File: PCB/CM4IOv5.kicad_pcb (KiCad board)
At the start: 6 copper layers, 80.9 x 63 mm, 67 parts, among them CN1 DF40C-100DS-0.4V(51), CN2 DF40C-100DS-0.4V(51), J1 Micro_SD_Card_Det, J2 Conn_01x02_Pin, J4 Conn_01x22_Female, J5 Conn_01x22_Female, U1 QG2439S, U2 74LVC1G07SE-7, U3 AP2331SA-7, U4 RT9742GGJ5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

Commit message: Routed EEPROM modules to SDA/SCL and GPIO pins.
These are definitely taking up more space than they need to, but a little extra space will provide easier in-situ changes if rewiring is needed.
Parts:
- removed R7: 523k, Resistor_SMD:R_0603_1608Metric
- removed R8: 84.5, Resistor_SMD:R_0603_1608Metric
- added U6: M24C64-WMN6TP, PARTS:SOIC-8_L5.0-W4.0-P1.27-LS6.0-BL, B.Cu at (429.3, 176.5)
- added U7: M24C64-WMN6TP, PARTS:SOIC-8_L5.0-W4.0-P1.27-LS6.0-BL, B.Cu at (418.8, 176.5)
- added U8: 74LVC1G125GV-TP, PARTS:SOT-23-5_L2.9-W1.6-P0.95-LS2.8-BR, B.Cu at (418.6, 172.0)
- added U9: 74LVC1G125GV-TP, PARTS:SOT-23-5_L2.9-W1.6-P0.95-LS2.8-BR, B.Cu at (429.5, 172.0)
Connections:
- RJ2 pad 5: /CM4_GPIO ( Ethernet, GPIO, SDCARD)/BI_DB- -> /CM4_GPIO ( Ethernet, GPIO, SDCARD)/BI_DC-
- RJ2 pad 6: Net-(RJ2-Pad6) -> /CM4_GPIO ( Ethernet, GPIO, SDCARD)/BI_DB-
- U1 pad 17: Net-(RJ2-Pad6) -> /CM4_GPIO ( Ethernet, GPIO, SDCARD)/BI_DB-
- U1 pad 20: /CM4_GPIO ( Ethernet, GPIO, SDCARD)/BI_DB- -> /CM4_GPIO ( Ethernet, GPIO, SDCARD)/BI_DC-
- U5 pad : (no net) -> GND
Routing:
- net /CM4_GPIO ( Ethernet, GPIO, SDCARD)/GPIO21: track 0.00 -> 47.6 mm, vias 0 -> 3
- net /CM4_HighSpeed/SDA0: track 60.5 -> 103.1 mm, vias 4 -> 9
- net /CM4_HighSpeed/SCL0: track 61.2 -> 101.8 mm, vias 4 -> 7
- net /CM4_GPIO ( Ethernet, GPIO, SDCARD)/GPIO25: track 0.00 -> 40.2 mm, vias 0 -> 3
- net /+3.3v: track 38.8 -> 70.6 mm, vias 10 -> 21
- net Net-(RJ2-Pad6): track 30.2 -> 0.00 mm, vias 1 -> 0
- net /CM4_GPIO ( Ethernet, GPIO, SDCARD)/BI_DC-: track 0.00 -> 23.8 mm
- net /CM4_GPIO ( Ethernet, GPIO, SDCARD)/ID_SC: track 89.8 -> 103.7 mm, vias 6 -> 9
- net /CM4_GPIO ( Ethernet, GPIO, SDCARD)/ID_SD: track 81.7 -> 93.5 mm, vias 3 -> 6
- net GND: track 172.6 -> 182.5 mm, vias 182 -> 169
- net Net-(U5-EN): track 7.31 -> 0.00 mm
- net /CM4_GPIO ( Ethernet, GPIO, SDCARD)/nPWR_LED: track 56.8 -> 63.9 mm
- net /CM4_GPIO ( Ethernet, GPIO, SDCARD)/BI_DB-: track 23.8 -> 30.2 mm, vias 0 -> 1
- net /CM4_GPIO ( Ethernet, GPIO, SDCARD)/PROM1_WC: track 0.00 -> 5.34 mm
- net /CM4_GPIO ( Ethernet, GPIO, SDCARD)/PROM0_WC: track 0.00 -> 5.13 mm
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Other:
- board text added: "PROM0"
- board text added: "PROM1"

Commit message: Updated fonts for export.
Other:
- board text added: "PROM_1"
- board text added: "PROM_Zero"
- board text removed: "PROM0"
- board text removed: "PROM1"

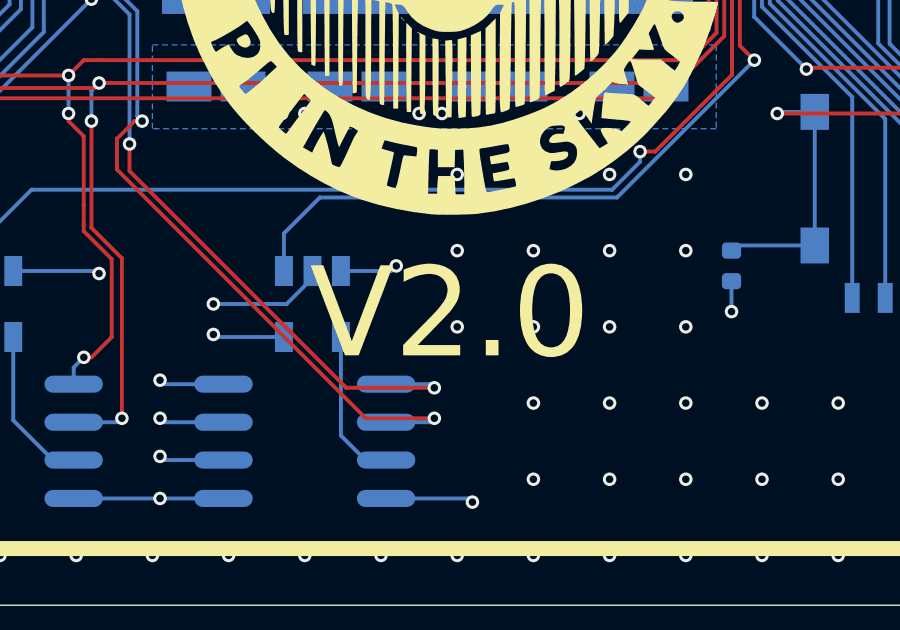
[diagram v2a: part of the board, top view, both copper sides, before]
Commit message: Updated silkscreen for release.
Exported STEP/JLC Production Files.
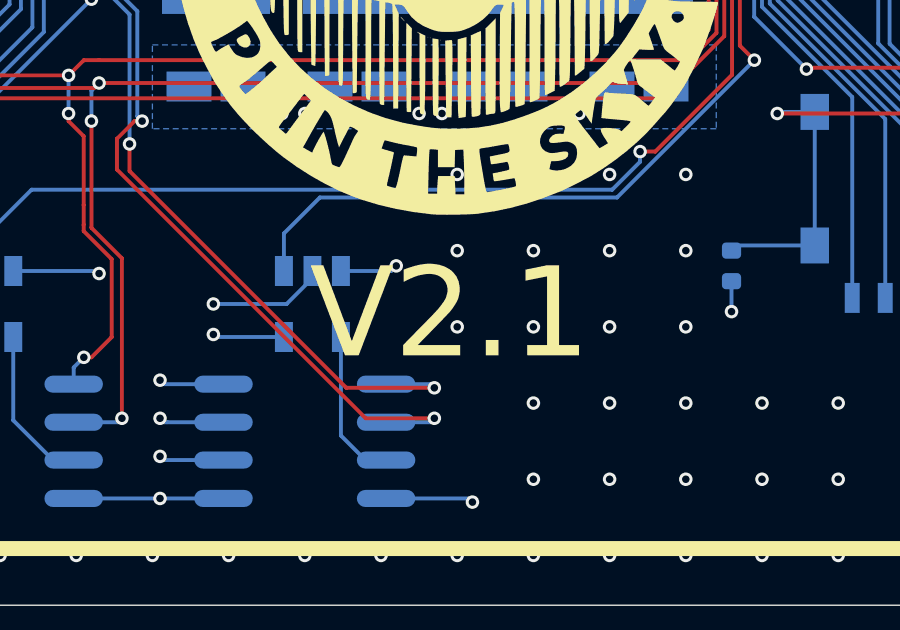
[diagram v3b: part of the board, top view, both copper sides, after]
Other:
- board text added: "V2.1"
- board text removed: "V2.0"
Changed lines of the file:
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@@
 			(pintype "unspecified")
 		)
-		(model "/PARTS.3dshapes/SOIC-8_L4.9-W3.9-H1.7-LS6.0-P1.27.wrl"
+		(model "${PARTS_3D_FILES}/SOIC-8_L4.9-W3.9-H1.7-LS6.0-P1.27.step"
 			(offset
 				(xyz 0 0 -0)
@@
 			(pintype "unspecified")
 		)
-		(model "/PARTS.3dshapes/SOIC-8_L4.9-W3.9-H1.7-LS6.0-P1.27.wrl"
+		(model "${PARTS_3D_FILES}/SOIC-8_L4.9-W3.9-H1.7-LS6.0-P1.27.step"
 			(offset
 				(xyz 0 0 -0)
@@
 		)
 	)
-	(gr_text "V2.0"
-		(at 407.065222 169.82 -0)
+	(gr_text "V2.1"
+		(at 407.065222 169.82 0)
 		(layer "B.SilkS" knockout)
 		(effects
@@
 			(justify mirror)
 		)
-		(render_cache "V2.0" -0
+		(render_cache "V2.1" 0
 			(polygon
 				(pts
@@
 			(polygon
 				(pts
-					(xy 403.960467 167.834354) (xy 404.113928 167.861041) (xy 404.263267 167.910603) (xy 404.358201 167.955574)
-					(xy 404.489783 168.039174) (xy 404.608382 168.142145) (xy 404.679823 168.221051) (xy 404.770498 168.349542)
-					(xy 404.84139 168.490191) (xy 404.876652 168.588881) (xy 404.910656 168.741552) (xy 404.92199 168.899787)
-					(xy 404.92199 170.041378) (xy 404.916952 170.147532) (xy 404.890505 170.302298) (xy 404.84139 170.451706)
-					(xy 404.796327 170.546502) (xy 404.712246 170.678737) (xy 404.608382 170.799019) (xy 404.530759 170.869819)
-					(xy 404.403504 170.959876) (xy 404.263267 171.030561) (xy 404.164165 171.066144) (xy 404.012078 171.100457)
-					(xy 403.85587 171.111894) (xy 403.751319 171.106811) (xy 403.598098 171.080123) (xy 403.449206 171.030561)
-					(xy 403.353951 170.985453) (xy 403.22206 170.901132) (xy 403.103358 170.796821) (xy 403.031962 170.717961)
-					(xy 402.941528 170.589711) (xy 402.871083 170.449508) (xy 402.8355 170.350635) (xy 402.801187 170.198376)
-					(xy 402.78975 170.041378) (xy 402.78975 168.924699) (xy 403.209603 168.924699) (xy 403.209603 170.022327)
-					(xy 403.214344 170.10868) (xy 403.246769 170.256182) (xy 403.309913 170.393482) (xy 403.403776 170.520582)
-					(xy 403.44062 170.559211) (xy 403.558027 170.652302) (xy 403.70058 170.715628) (xy 403.85587 170.736737)
-					(xy 403.903801 170.734837) (xy 404.055384 170.701063) (xy 404.194373 170.625071) (xy 404.308696 170.520582)
-					(xy 404.364424 170.451231) (xy 404.440931 170.318464) (xy 404.486835 170.175496) (xy 404.502136 170.022327)
-					(xy 404.502136 168.924699) (xy 404.497378 168.838486) (xy 404.46483 168.690784) (xy 404.401448 168.552704)
-					(xy 404.307231 168.424246) (xy 404.270145 168.384962) (xy 404.152396 168.290294) (xy 404.010144 168.225894)
-					(xy 403.85587 168.204427) (xy 403.808326 168.206353) (xy 403.657658 168.240585) (xy 403.519012 168.317607)
-					(xy 403.404509 168.423513) (xy 403.348359 168.493323) (xy 403.271273 168.626914) (xy 403.225021 168.770706)
-					(xy 403.209603 168.924699) (xy 402.78975 168.924699) (xy 402.78975 168.899787) (xy 402.794833 168.793678)
-					(xy 402.82152 168.639153) (xy 402.871083 168.490191) (xy 402.915825 168.395074) (xy 402.999596 168.26253)
-					(xy 403.103358 168.142145) (xy 403.181027 168.071345) (xy 403.308522 167.981289) (xy 403.449206 167.910603)
-					(xy 403.547986 167.87502) (xy 403.699764 167.840708) (xy 403.85587 167.82927)
+					(xy 403.974572 168.315069) (xy 404.025863 168.251322) (xy 404.458905 168.251322) (xy 404.36072 167.876165)
+					(xy 403.924014 167.876165) (xy 403.778845 167.898222) (xy 403.653637 167.976549) (xy 403.576453 168.103679)
+					(xy 403.554718 168.249856) (xy 403.554718 171.065) (xy 403.974572 171.065)
 				)
 			)
@@
 		)
 	)
-	(gr_text "V2.0"
+	(gr_text "V2.1"
 		(at 434.1 172.28 0)
 		(layer "F.SilkS" knockout)
@@
 			)
 		)
-		(render_cache "V2.0" 0
+		(render_cache "V2.1" 0
 			(polygon
 				(pts
@@
 			(polygon
 				(pts
-					(xy 437.465457 170.300708) (xy 437.617235 170.33502) (xy 437.716015 170.370603) (xy 437.856699 170.441289)
-					(xy 437.984194 170.531345) (xy 438.061863 170.602145) (xy 438.165625 170.72253) (xy 438.249396 170.855074)
-					(xy 438.294138 170.950191) (xy 438.343701 171.099153) (xy 438.370388 171.253678) (xy 438.375471 171.359787)
-					(xy 438.375471 172.501378) (xy 438.364034 172.658376) (xy 438.329721 172.810635) (xy 438.294138 172.909508)
-					(xy 438.223693 173.049711) (xy 438.133259 173.177961) (xy 438.061863 173.256821) (xy 437.943161 173.361132)
-					(xy 437.81127 173.445453) (xy 437.716015 173.490561) (xy 437.567123 173.540123) (xy 437.413902 173.566811)
-					(xy 437.309351 173.571894) (xy 437.153143 173.560457) (xy 437.001056 173.526144) (xy 436.901954 173.490561)
-					(xy 436.761717 173.419876) (xy 436.634462 173.329819) (xy 436.556839 173.259019) (xy 436.452975 173.138737)
-					(xy 436.368894 173.006502) (xy 436.323831 172.911706) (xy 436.274716 172.762298) (xy 436.248269 172.607532)
-					(xy 436.243231 172.501378) (xy 436.243231 171.384699) (xy 436.663085 171.384699) (xy 436.663085 172.482327)
-					(xy 436.678386 172.635496) (xy 436.72429 172.778464) (xy 436.800797 172.911231) (xy 436.856525 172.980582)
-					(xy 436.970848 173.085071) (xy 437.109837 173.161063) (xy 437.26142 173.194837) (xy 437.309351 173.196737)
-					(xy 437.464641 173.175628) (xy 437.607194 173.112302) (xy 437.724601 173.019211) (xy 437.761445 172.980582)
-					(xy 437.855308 172.853482) (xy 437.918452 172.716182) (xy 437.950877 172.56868) (xy 437.955618 172.482327)
-					(xy 437.955618 171.384699) (xy 437.9402 171.230706) (xy 437.893948 171.086914) (xy 437.816862 170.953323)
-					(xy 437.760712 170.883513) (xy 437.646209 170.777607) (xy 437.507563 170.700585) (xy 437.356895 170.666353)
-					(xy 437.309351 170.664427) (xy 437.155077 170.685894) (xy 437.012825 170.750294) (xy 436.895076 170.844962)
-					(xy 436.85799 170.884246) (xy 436.763773 171.012704) (xy 436.700391 171.150784) (xy 436.667843 171.298486)
-					(xy 436.663085 171.384699) (xy 436.243231 171.384699) (xy 436.243231 171.359787) (xy 436.254565 171.201552)
-					(xy 436.288569 171.048881) (xy 436.323831 170.950191) (xy 436.394723 170.809542) (xy 436.485398 170.681051)
-					(xy 436.556839 170.602145) (xy 436.675438 170.499174) (xy 436.80702 170.415574) (xy 436.901954 170.370603)
-					(xy 437.051293 170.321041) (xy 437.204754 170.294354) (xy 437.309351 170.28927)
+					(xy 437.190649 170.775069) (xy 437.139358 170.711322) (xy 436.706316 170.711322) (xy 436.804501 170.336165)
+					(xy 437.241207 170.336165) (xy 437.386376 170.358222) (xy 437.511584 170.436549) (xy 437.588768 170.563679)
+					(xy 437.610503 170.709856) (xy 437.610503 173.525) (xy 437.190649 173.525)
 				)
 			)

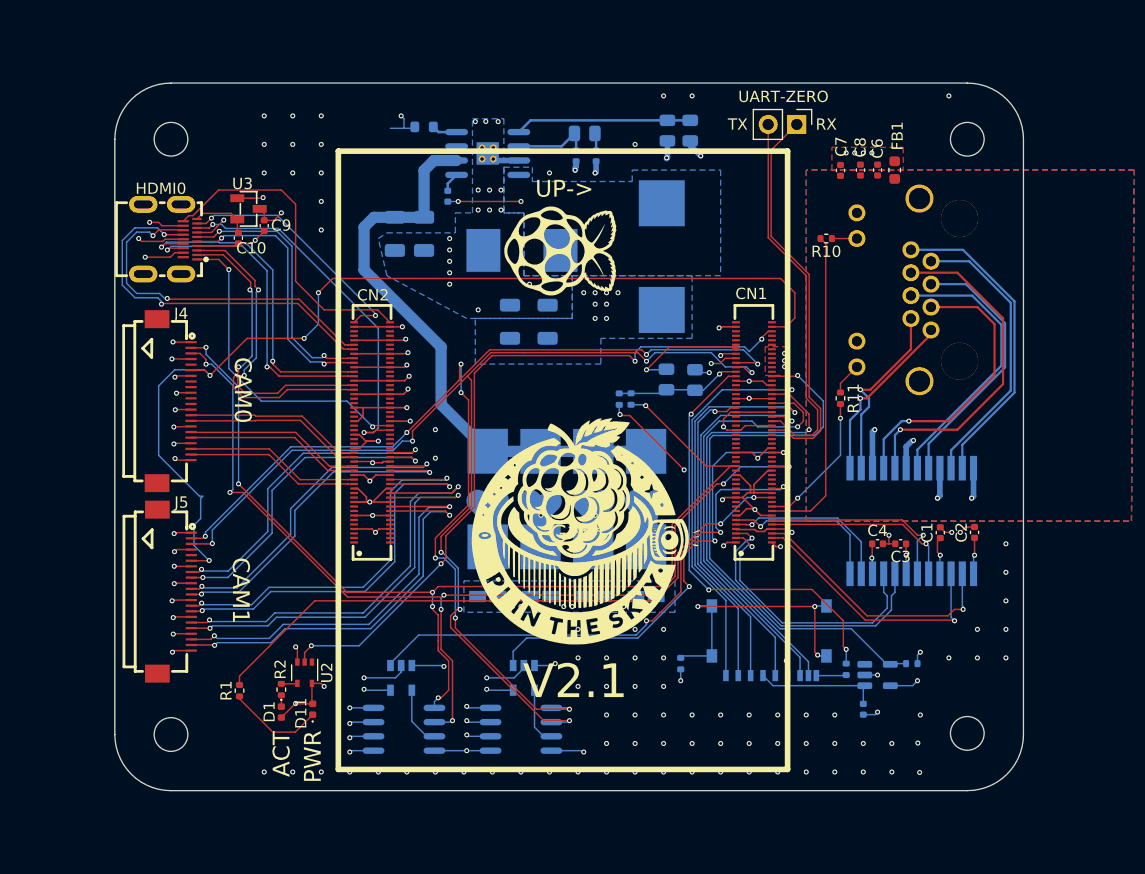
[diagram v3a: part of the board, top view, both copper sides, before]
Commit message: Fixed hole connected to every plain.
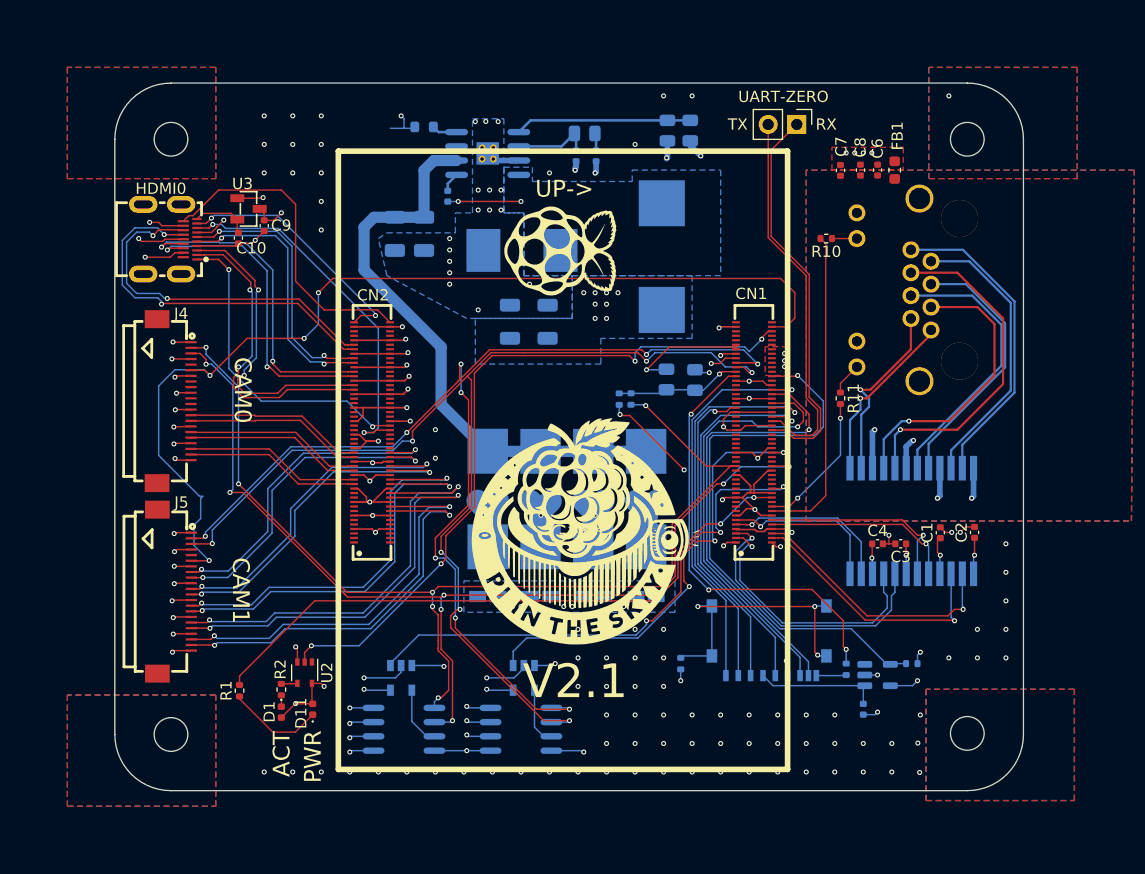
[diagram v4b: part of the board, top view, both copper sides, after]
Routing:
- added copper zone on B.Cu, net (none)
- added copper zone on F.Cu, net (none)
- added copper zone on In1.Cu, net (none)
- added copper zone on In2.Cu, net (none)
- added copper zone on In3.Cu, net (none)
- added copper zone on In4.Cu, net (none)
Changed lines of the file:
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@@
+	)
+	(zone
+		(net 0)
+		(net_name "")
+		(layers "F.Cu" "In1.Cu" "In2.Cu" "In3.Cu" "In4.Cu" "B.Cu")
+		(hatch edge 0.5)
+		(priority 100)
+		(connect_pads
+			(clearance 0.5)
+		)
+		(min_thickness 0.25)
+		(filled_areas_thickness no)
+		(fill yes
+			(thermal_gap 0.5)
+			(thermal_bridge_width 0.5)
+			(island_removal_mode 1)
+			(island_area_min 10)
+		)
+		(polygon
+			(pts
+				(xy 465.582 117.602) (xy 465.582 127.508) (xy 478.79 127.508) (xy 478.79 117.602)
+			)
+		)
+	)
+	(zone
+		(net 0)
+		(net_name "")
+		(layers "F.Cu" "In1.Cu" "In2.Cu" "In3.Cu" "In4.Cu" "B.Cu")
+		(hatch edge 0.5)
+		(priority 100)
+		(connect_pads
+			(clearance 0.5)
+		)
+		(min_thickness 0.25)
+		(filled_areas_thickness no)
+		(fill yes
+			(thermal_gap 0.5)
+			(thermal_bridge_width 0.5)
+			(island_removal_mode 1)
+			(island_area_min 10)
+		)
+		(polygon
+			(pts
+				(xy 388.874 173.482) (xy 388.874 183.388) (xy 402.082 183.388) (xy 402.082 173.482)
+			)
+		)
+	)
+	(zone
+		(net 0)
+		(net_name "")
+		(layers "F.Cu" "In1.Cu" "In2.Cu" "In3.Cu" "In4.Cu" "B.Cu")
+		(hatch edge 0.5)
+		(priority 100)
+		(connect_pads
+			(clearance 0.5)
+		)
+		(min_thickness 0.25)
+		(filled_areas_thickness no)
+		(fill yes
+			(thermal_gap 0.5)
+			(thermal_bridge_width 0.5)
+			(island_removal_mode 1)
+			(island_area_min 10)
+		)
+		(polygon
+			(pts
+				(xy 388.874 117.602) (xy 388.874 127.508) (xy 402.082 127.508) (xy 402.082 117.602)
+			)
+		)
 	)
 	(zone
@@
 			)
 		)
+	)
+	(zone
+		(net 0)
+		(net_name "")
+		(layers "F.Cu" "In1.Cu" "In2.Cu" "In3.Cu" "In4.Cu" "B.Cu")
+		(hatch edge 0.5)
+		(priority 100)
+		(connect_pads
+			(clearance 0.5)
+		)
+		(min_thickness 0.25)
+		(filled_areas_thickness no)
+		(fill yes
+			(thermal_gap 0.5)
+			(thermal_bridge_width 0.5)
+			(island_removal_mode 1)
+			(island_area_min 10)
+		)
+		(polygon
+			(pts
+				(xy 465.328 172.974) (xy 465.328 182.88) (xy 478.536 182.88) (xy 478.536 172.974)
+			)
+		)
